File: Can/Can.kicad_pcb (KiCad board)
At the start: 2 copper layers, 8 parts

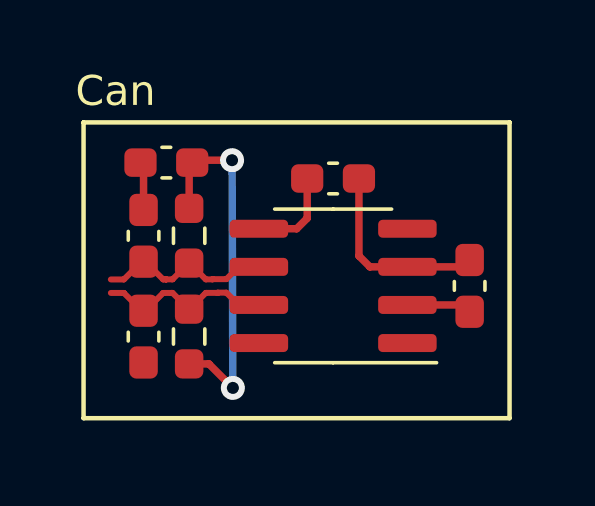
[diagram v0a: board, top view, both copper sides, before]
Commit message: add power 12+ and 12-
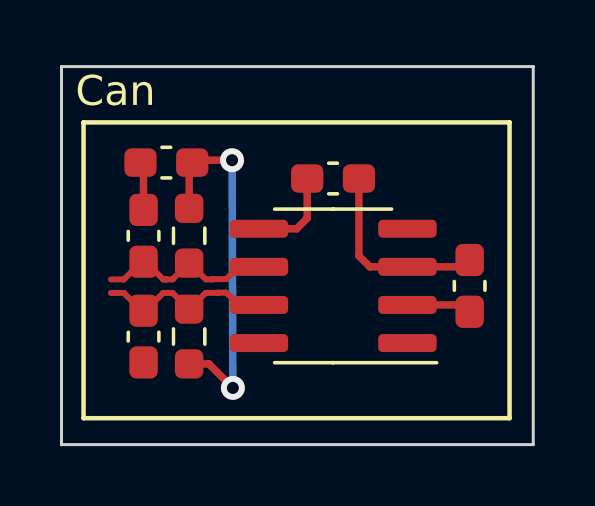
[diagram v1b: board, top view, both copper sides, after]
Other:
- board outline added: 15.7 x 12.6 mm
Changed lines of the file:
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@@
   (gr_rect (start 141.51 81.11) (end 155.71 90.97)
     (stroke (width 0.15) (type default)) (fill none) (layer "F.SilkS"))
+  (gr_rect (start 140.775 79.25) (end 156.5 91.85)
+    (stroke (width 0.1) (type default)) (fill none) (layer "Edge.Cuts"))
   (gr_text "Can" (at 141.24 80.65) (layer "F.SilkS")
     (effects (font (size 1 1) (thickness 0.15)) (justify left bottom))
